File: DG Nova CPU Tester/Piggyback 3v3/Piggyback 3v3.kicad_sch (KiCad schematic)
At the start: 19 parts, among them J10 Programmed I/O, J11 CPU Option Inputs, J12 Data Channel, J13 Program Interrupt, J14 System Control, J17 CPU Option Outputs, J18 MEM Control Outputs, J19 Logic 8 CH, J20 Logic 8 CH, J6 MBO, J7 MEM, J8 Data Channel, J9 Front Panel Controls, U1 74LS125, U2 Pico

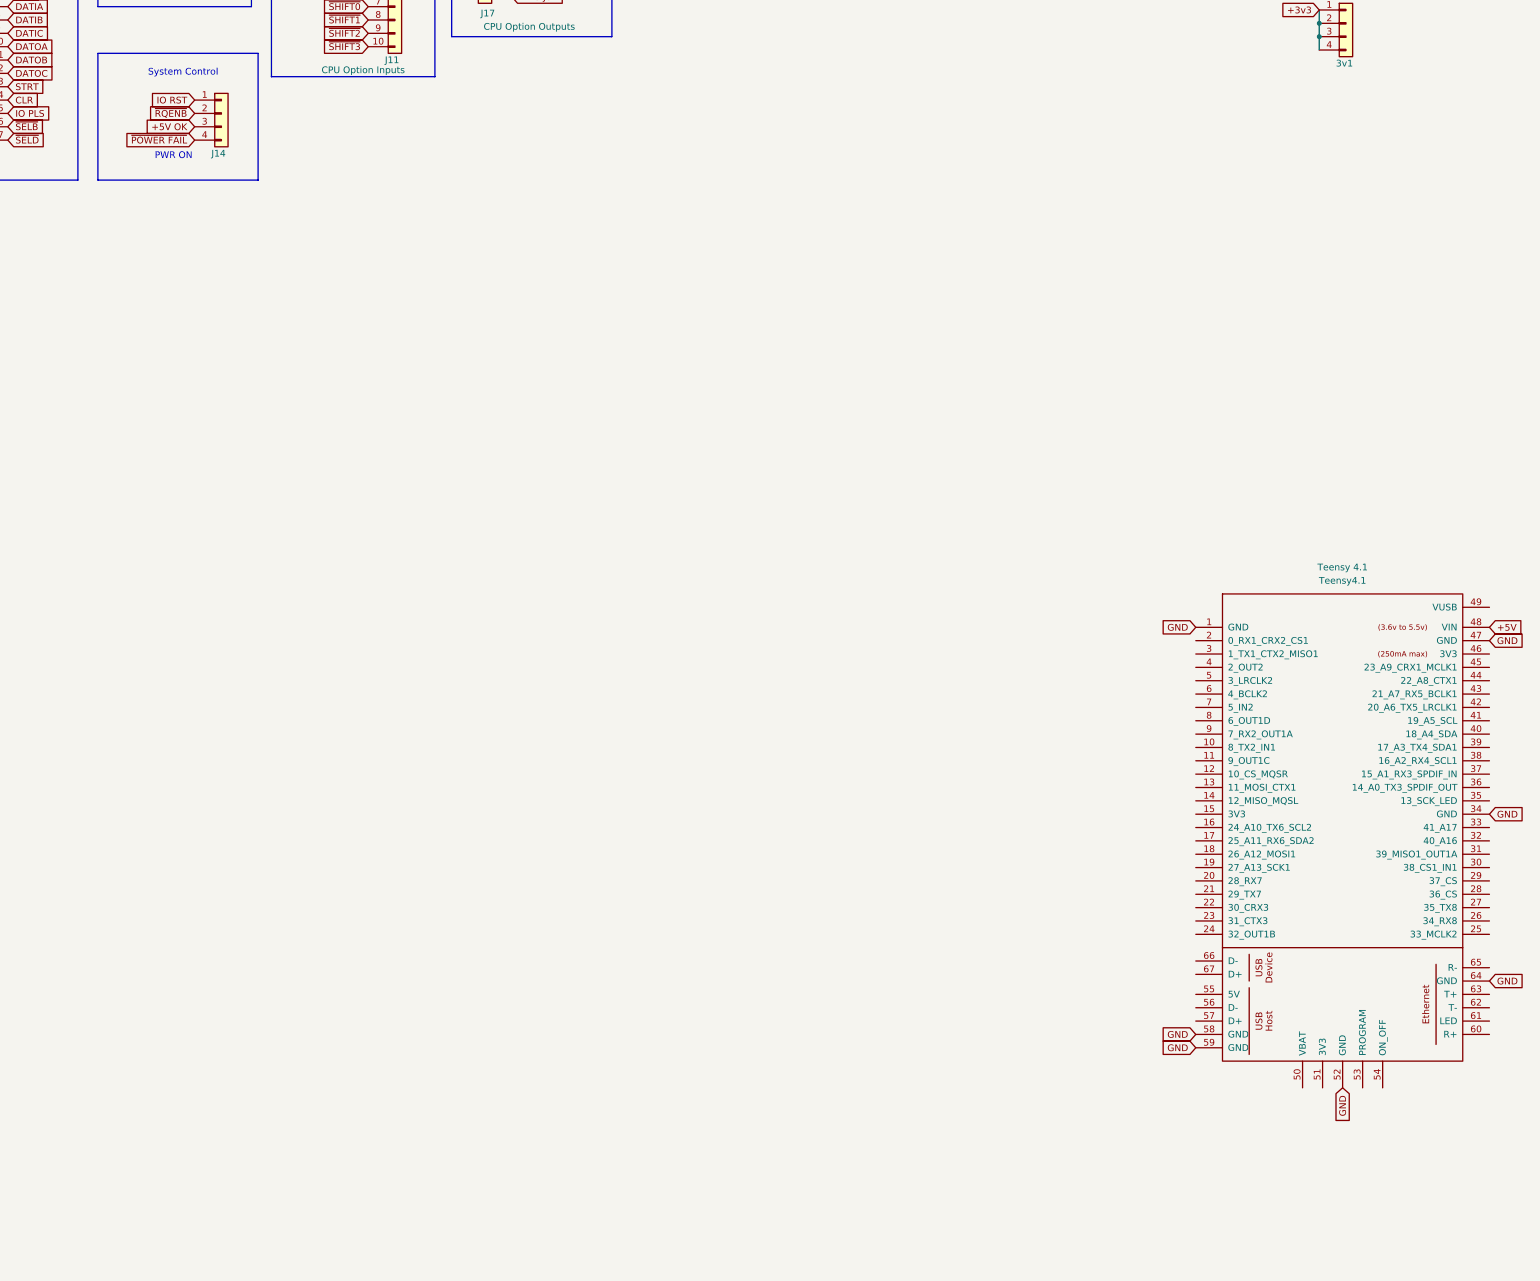
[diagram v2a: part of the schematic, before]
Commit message: 3v3 to 5v work
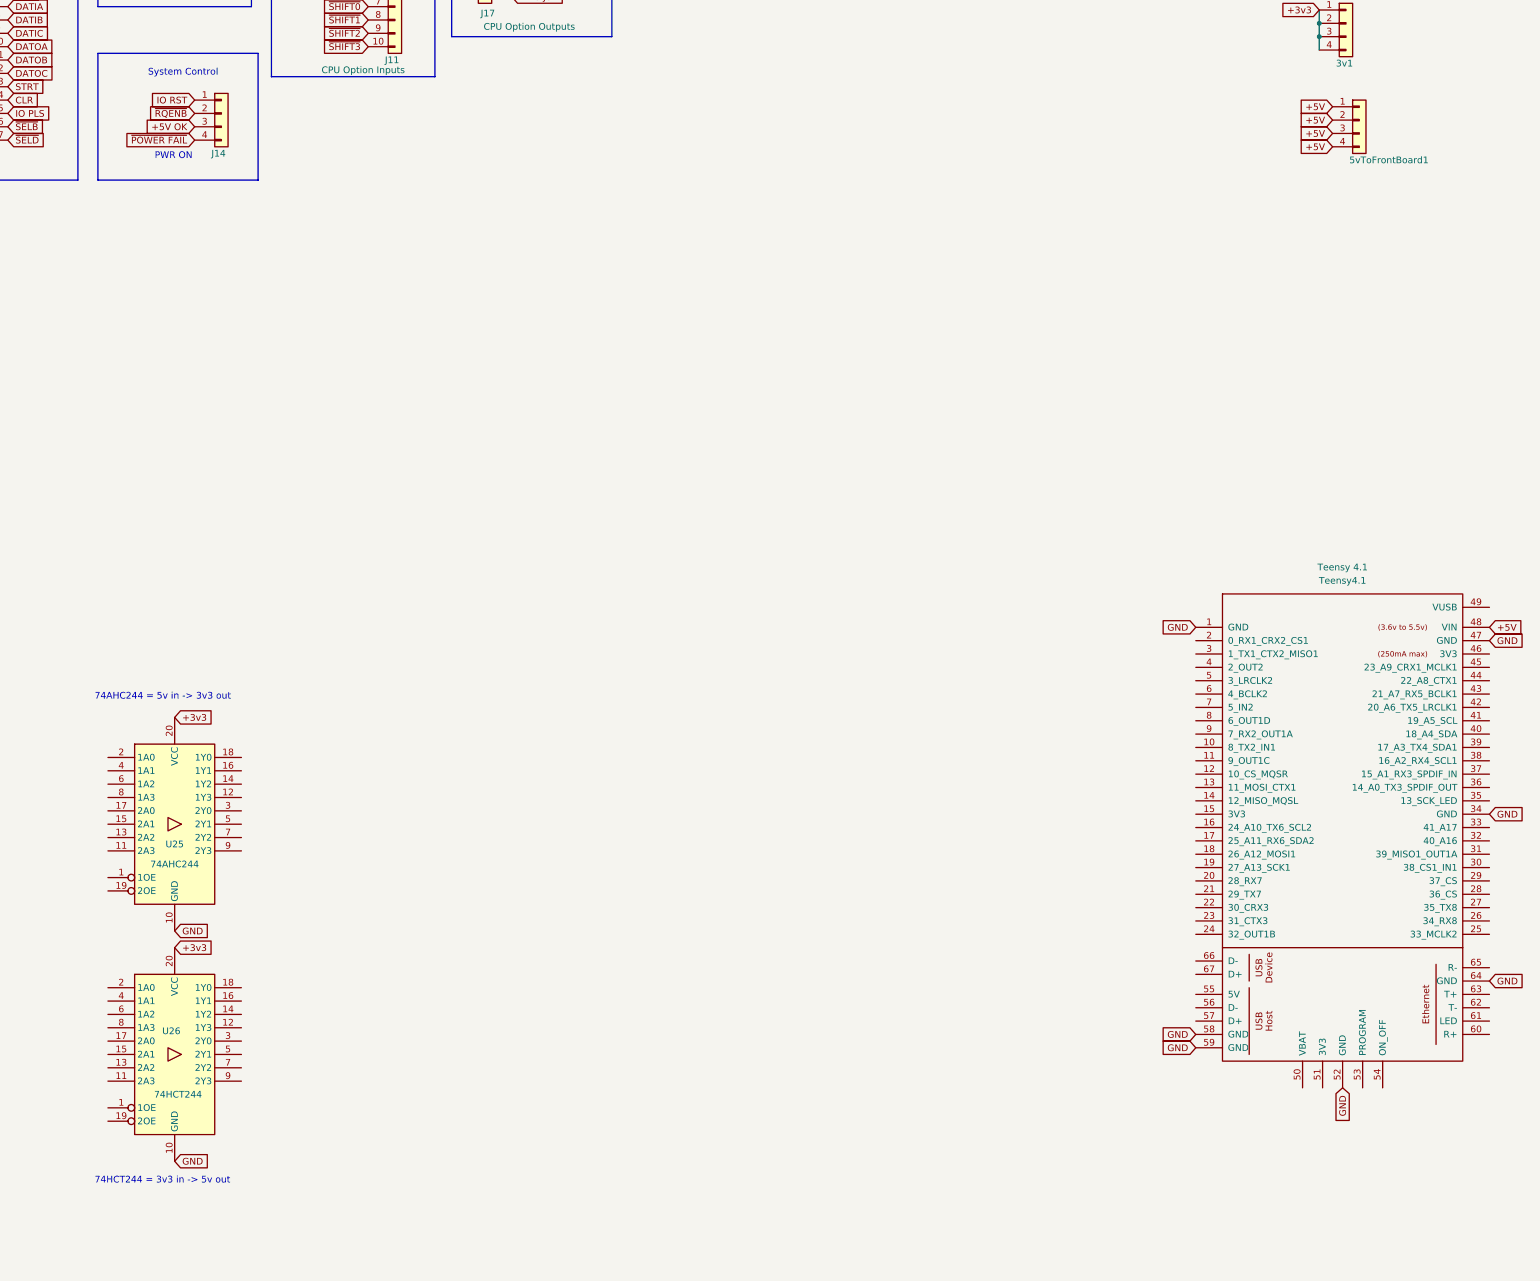
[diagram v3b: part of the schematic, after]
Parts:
- added 5vToFrontBoard1: 3v3, Connector_PinHeader_2.54mm:PinHeader_1x04_P2.54mm_Vertical, symbol Connector_Generic:Conn_01x04
- added U25: 74AHC244, Package_DIP:DIP-20_W7.62mm_Socket_LongPads, symbol 74xx:74HCT244
- added U26: 74HCT244, Package_DIP:DIP-20_W7.62mm_Socket_LongPads, symbol 74xx:74HCT244
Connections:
- net +3v3: now also U25.20 (VCC), U26.20 (VCC)
- net +5V: now also 5vToFrontBoard1.1 (Pin_1), 5vToFrontBoard1.2 (Pin_2), 5vToFrontBoard1.3 (Pin_3), 5vToFrontBoard1.4 (Pin_4)
- net GND: now also U25.10 (GND), U26.10 (GND)
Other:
- note added: "74AHC244 = 5v in -> 3v3 out"
- note added: "74HCT244 = 3v3 in -> 5v out"
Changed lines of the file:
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@@
+    (effects (font (size 1.27 1.27)) (justify left bottom))
+  )
+  (text "74HCT244 = 3v3 in -> 5v out\n" (at 209.55 263.525 0)
     (effects (font (size 1.27 1.27)) (justify left bottom))
   )
@@
     (effects (font (size 1.27 1.27)) (justify right bottom))
   )
+  (text "74AHC244 = 5v in -> 3v3 out" (at 209.55 171.45 0)
+    (effects (font (size 1.27 1.27)) (justify left bottom))
+  )
   (text "System Control\n" (at 219.71 52.705 0)
     (effects (font (size 1.27 1.27)) (justify left bottom))
@@
     (effects (font (size 1.27 1.27)) (justify left))
     (property "Intersheetrefs" "${INTERSHEET_REFS}" (at 71.5271 328.93 0)
+      (effects (font (size 1.27 1.27)) (justify left) hide)
+    )
+  )
+  (global_label "GND" (shape input) (at 224.79 215.265 0) (fields_autoplaced)
+    (effects (font (size 1.27 1.27)) (justify left))
+    (property "Intersheetrefs" "${INTERSHEET_REFS}" (at 230.9915 215.265 0)
       (effects (font (size 1.27 1.27)) (justify left) hide)
     )
@@
     )
   )
+  (global_label "+5V" (shape input) (at 445.135 66.04 180) (fields_autoplaced)
+    (effects (font (size 1.27 1.27)) (justify right))
+    (property "Intersheetrefs" "${INTERSHEET_REFS}" (at 438.9335 66.04 0)
+      (effects (font (size 1.27 1.27)) (justify right) hide)
+    )
+  )
   (global_label "Logic2" (shape input) (at 65.405 318.77 0) (fields_autoplaced)
     (effects (font (size 1.27 1.27)) (justify left))
@@
     )
   )
+  (global_label "+5V" (shape input) (at 445.135 58.42 180) (fields_autoplaced)
+    (effects (font (size 1.27 1.27)) (justify right))
+    (property "Intersheetrefs" "${INTERSHEET_REFS}" (at 438.9335 58.42 0)
+      (effects (font (size 1.27 1.27)) (justify right) hide)
+    )
+  )
   (global_label "UART_RX" (shape input) (at 87.63 184.785 180) (fields_autoplaced)
     (effects (font (size 1.27 1.27)) (justify right))
@@
     )
   )
+  (global_label "GND" (shape input) (at 224.79 259.08 0) (fields_autoplaced)
+    (effects (font (size 1.27 1.27)) (justify left))
+    (property "Intersheetrefs" "${INTERSHEET_REFS}" (at 230.9915 259.08 0)
+      (effects (font (size 1.27 1.27)) (justify left) hide)
+    )
+  )
   (global_label "+3v3" (shape input) (at 141.605 184.785 0) (fields_autoplaced)
     (effects (font (size 1.27 1.27)) (justify left))
@@
     )
   )
+  (global_label "+3v3" (shape input) (at 224.79 174.625 0) (fields_autoplaced)
+    (effects (font (size 1.27 1.27)) (justify left))
+    (property "Intersheetrefs" "${INTERSHEET_REFS}" (at 232.08 174.625 0)
+      (effects (font (size 1.27 1.27)) (justify left) hide)
+    )
+  )
   (global_label "~{DCHM1}" (shape input) (at 160.02 33.655 0) (fields_autoplaced)
     (effects (font (size 1.27 1.27)) (justify left))
@@
     )
   )
+  (global_label "+3v3" (shape input) (at 224.79 218.44 0) (fields_autoplaced)
+    (effects (font (size 1.27 1.27)) (justify left))
+    (property "Intersheetrefs" "${INTERSHEET_REFS}" (at 232.08 218.44 0)
+      (effects (font (size 1.27 1.27)) (justify left) hide)
+    )
+  )
   (global_label "~{READ1}" (shape input) (at 106.68 29.845 0) (fields_autoplaced)
     (effects (font (size 1.27 1.27)) (justify left))
@@
     )
   )
+  (global_label "+5V" (shape input) (at 445.135 63.5 180) (fields_autoplaced)
+    (effects (font (size 1.27 1.27)) (justify right))
+    (property "Intersheetrefs" "${INTERSHEET_REFS}" (at 438.9335 63.5 0)
+      (effects (font (size 1.27 1.27)) (justify right) hide)
+    )
+  )
   (global_label "~{MEM6}" (shape input) (at 79.375 38.1 0) (fields_autoplaced)
     (effects (font (size 1.27 1.27)) (justify left))
@@
     (property "Intersheetrefs" "${INTERSHEET_REFS}" (at 200.4926 44.45 0)
       (effects (font (size 1.27 1.27)) (justify left) hide)
+    )
+  )
+  (global_label "+5V" (shape input) (at 445.135 60.96 180) (fields_autoplaced)
+    (effects (font (size 1.27 1.27)) (justify right))
+    (property "Intersheetrefs" "${INTERSHEET_REFS}" (at 438.9335 60.96 0)
+      (effects (font (size 1.27 1.27)) (justify right) hide)
     )
   )
@@
     )
   )
+  (symbol (lib_id "74xx:74HCT244") (at 224.79 238.76 0) (unit 1)
+    (in_bom yes) (on_board yes) (dnp no)
+    (property "Reference" "U26" (at 224.155 234.315 0)
+      (effects (font (size 1.27 1.27)))
+    )
+    (property "Value" "74HCT244" (at 225.425 246.38 0)
+      (effects (font (size 1.27 1.27)))
+    )
+    (property "Footprint" "Package_DIP:DIP-20_W7.62mm_Socket_LongPads" (at 224.79 238.76 0)
+      (effects (font (size 1.27 1.27)) hide)
+    )
+    (property "Datasheet" "https://assets.nexperia.com/documents/data-sheet/74HC_HCT244.pdf" (at 224.79 238.76 0)
+      (effects (font (size 1.27 1.27)) hide)
+    )
+    (pin "1")
+    (pin "10")
+    (pin "11")
+    (pin "12")
+    (pin "13")
+    (pin "14")
+    (pin "15")
+    (pin "16")
+    (pin "17")
+    (pin "18")
+    (pin "19")
+    (pin "2")
+    (pin "20")
+    (pin "3")
+    (pin "4")
+    (pin "5")
+    (pin "6")
+    (pin "7")
+    (pin "8")
+    (pin "9")
+    (instances
+      (project "FeRAM v0"
+        (path "/28841cc8-873e-459e-b605-cedf187751a5"
+          (reference "U26") (unit 1)
+        )
+      )
+      (project "Piggyback 3v3"
+        (path "/c1f710ce-b3f9-4828-9325-9c2326e8d74c"
+          (reference "U3") (unit 1)
+        )
+      )
+    )
+  )
   (symbol (lib_id "Connector_Generic:Conn_01x04") (at 229.235 26.67 0) (unit 1)
     (in_bom yes) (on_board yes) (dnp no)
@@
     )
   )
+  (symbol (lib_id "74xx:74HCT244") (at 224.79 194.945 0) (unit 1)
+    (in_bom yes) (on_board yes) (dnp no)
+    (property "Reference" "U25" (at 224.79 198.755 0)
+      (effects (font (size 1.27 1.27)))
+    )
+    (property "Value" "74AHC244" (at 224.79 202.565 0)
+      (effects (font (size 1.27 1.27)))
+    )
+    (property "Footprint" "Package_DIP:DIP-20_W7.62mm_Socket_LongPads" (at 224.79 194.945 0)
+      (effects (font (size 1.27 1.27)) hide)
+    )
+    (property "Datasheet" "https://assets.nexperia.com/documents/data-sheet/74HC_HCT244.pdf" (at 224.79 194.945 0)
+      (effects (font (size 1.27 1.27)) hide)
+    )
+    (pin "1")
+    (pin "10")
+    (pin "11")
+    (pin "12")
+    (pin "13")
+    (pin "14")
+    (pin "15")
+    (pin "16")
+    (pin "17")
+    (pin "18")
+    (pin "19")
+    (pin "2")
+    (pin "20")
+    (pin "3")
+    (pin "4")
+    (pin "5")
+    (pin "6")
+    (pin "7")
+    (pin "8")
+    (pin "9")
+    (instances
+      (project "FeRAM v0"
+        (path "/28841cc8-873e-459e-b605-cedf187751a5"
+          (reference "U25") (unit 1)
+        )
+      )
+      (project "Piggyback 3v3"
+        (path "/c1f710ce-b3f9-4828-9325-9c2326e8d74c"
+          (reference "U4") (unit 1)
+        )
+      )
+    )
+  )
   (symbol (lib_id "Connector_Generic:Conn_01x08") (at 57.785 301.625 90) (unit 1)
     (in_bom yes) (on_board yes) (dnp no)
@@
         )
       )
+    )
+  )
+  (symbol (lib_id "Connector_Generic:Conn_01x04") (at 450.215 60.96 0) (unit 1)
+    (in_bom yes) (on_board yes) (dnp no)
+    (property "Reference" "5vToFrontBoard1" (at 448.31 68.58 0)
+      (effects (font (size 1.27 1.27)) (justify left))
+    )
+    (property "Value" "3v3" (at 452.755 64.135 0)
+      (effects (font (size 1.27 1.27)) (justify left) hide)
+    )
+    (property "Footprint" "Connector_PinHeader_2.54mm:PinHeader_1x04_P2.54mm_Vertical" (at 450.215 60.96 0)
+      (effects (font (size 1.27 1.27)) hide)
+    )
+    (property "Datasheet" "~" (at 450.215 60.96 0)
+      (effects (font (size 1.27 1.27)) hide)
+    )
+    (pin "1")
+    (pin "2")
+    (pin "3")
+    (pin "4")
+    (instances
+      (project "Piggyback 3v3"
+        (path "/c1f710ce-b3f9-4828-9325-9c2326e8d74c"
+          (reference "5vToFrontBoard1") (unit 1)
+        )
+      )

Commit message: GPIO research
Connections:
- no-connect marks 0 -> 55
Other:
- note added: "A"
- note added: "B"
